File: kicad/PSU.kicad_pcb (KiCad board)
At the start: 2 copper layers, 91.4 x 105.4 mm, 74 parts, among them J1 +12V in1, J10 0V, J11 +5Vu, J2 +12V in2, J3 0v, J4 Conn_02x20_Odd_Even, J5 LED-, J6 LED+, J7 Sw, J8 Sw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

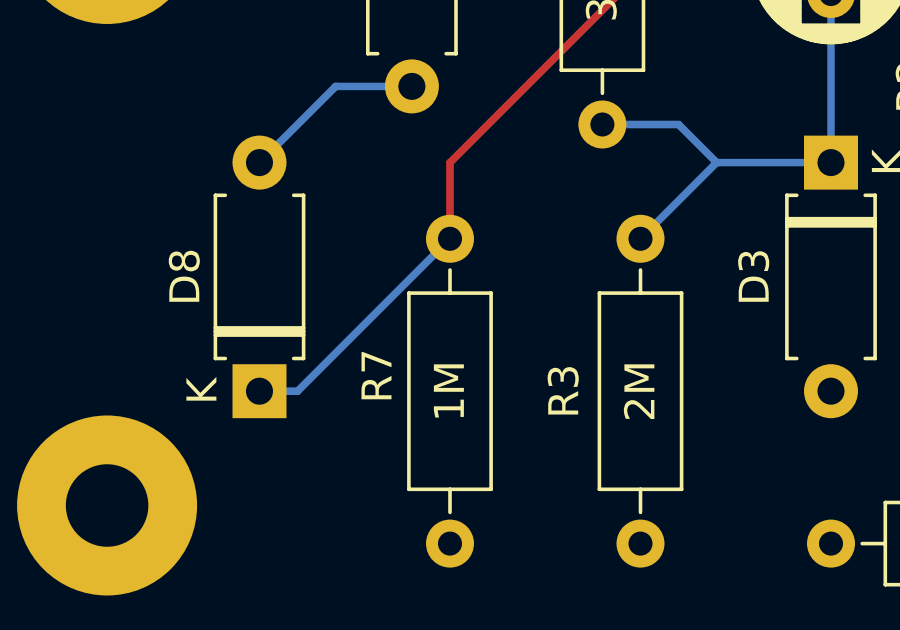
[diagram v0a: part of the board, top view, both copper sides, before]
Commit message: Initial release of revision 2.  Fixes from prototyping and experiments.
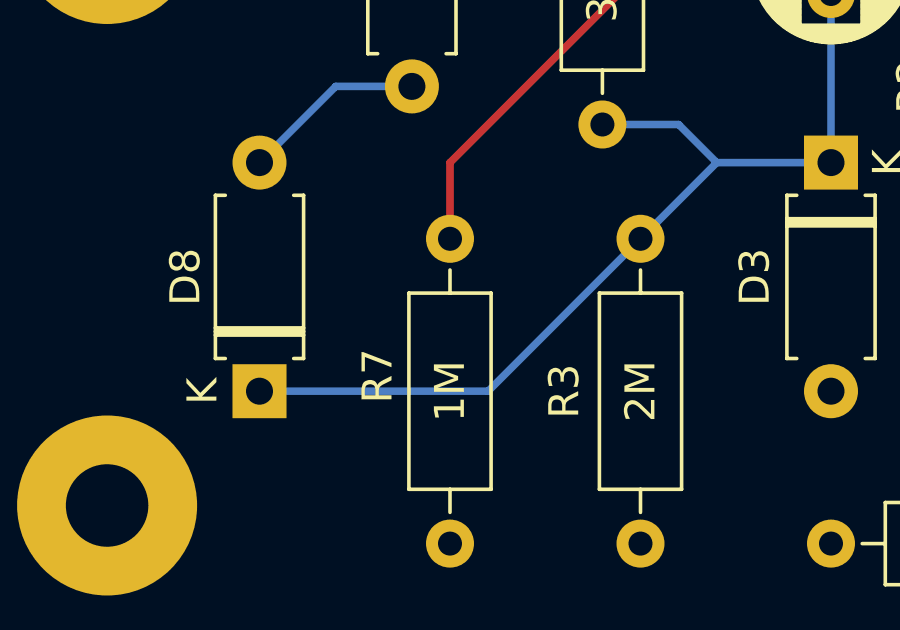
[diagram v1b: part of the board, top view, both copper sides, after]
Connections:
- C1 pad 2: Net-(C1-Pad2) -> Net-(D8-Pad1)
- D3 pad 1: Net-(C1-Pad2) -> Net-(D8-Pad1)
- R12 pad 1: Net-(D8-Pad1) -> Net-(R12-Pad1)
- R3 pad 1: Net-(C1-Pad2) -> Net-(D8-Pad1)
- R4 pad 1: Net-(C1-Pad2) -> Net-(D8-Pad1)
- R6 pad 2: Net-(D8-Pad1) -> Net-(R12-Pad1)
- R7 pad 1: Net-(D8-Pad1) -> Net-(R12-Pad1)
- U1 pad 5: Net-(D8-Pad1) -> Net-(R12-Pad1)
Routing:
- net Net-(R12-Pad1): track 0.00 -> 48.4 mm
- net Net-(D8-Pad1): track 56.9 -> 32.2 mm
- net Net-(C1-Pad2): track 17.4 -> 0.00 mm
